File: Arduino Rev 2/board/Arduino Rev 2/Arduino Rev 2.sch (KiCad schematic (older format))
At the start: 0 parts

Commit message: finished Schematic
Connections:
- net labels added: D0_RX, D1_TX, RESET
- wire segments 4 -> 34
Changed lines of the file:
@@
 $Descr A4 11693 8268
 encoding utf-8
-Sheet 1 4
+Sheet 1 6
 Title ""
 Date ""
@@
 F19 "A4_SDA" I R 6450 4450 50
 F20 "A5_SCL" I R 6450 4550 50
-F21 "RESET" I L 4900 4600 50
+F21 "RESET" I L 4900 4500 50
 F22 "D0_RX" I L 4900 3250 50
 F23 "D1_TX" I L 4900 3350 50
@@
 F2 "TXD" I R 4000 3350 50
 F3 "RXD" I R 4000 3250 50
+F4 "DTR" I R 4000 3800 50
 $EndSheet
 Wire Wire Line
@@
 F0 "RESET" 50
 F1 "RESET.sch" 50
+F2 "RESET" I R 4050 4500 50
 $EndSheet
+Wire Wire Line
+	4050 4500 4500 4500
+Wire Wire Line
+	4000 3800 4500 3800
+Wire Wire Line
+	4500 3800 4500 4500
+Connection ~ 4500 4500
+Wire Wire Line
+	4500 4500 4900 4500
+Text Label 4150 4500 0    50   ~ 0
+RESET
+$Sheet
+S 7250 2500 1050 2700
+U 5F10049F
+F0 "PIN HEADERS" 50
+F1 "PIN HEADERS.sch" 50
+F2 "1" I L 7250 2550 50
+F3 "2" I L 7250 2650 50
+F4 "3" I L 7250 2750 50
+F5 "4" I L 7250 2850 50
+F6 "5" I L 7250 2950 50
+F7 "6" I L 7250 3050 50
+F8 "7" I L 7250 3150 50
+F9 "8" I L 7250 3250 50
+F10 "9" I L 7250 3350 50
+F11 "10" I L 7250 3450 50
+F12 "11" I L 7250 3550 50
+F13 "12" I L 7250 3650 50
+F14 "13" I L 7250 3750 50
+F15 "14" I L 7250 3850 50
+F16 "15" I L 7250 4050 50
+F17 "16" I L 7250 4150 50
+F18 "17" I L 7250 4250 50
+F19 "18" I L 7250 4350 50
+F20 "19" I L 7250 4450 50
+F21 "20" I L 7250 4550 50
+F22 "21" I L 7250 4650 50
+F23 "22" I L 7250 4750 50
+F24 "23" I L 7250 5000 50
+F25 "24" I L 7250 5100 50
+$EndSheet
+Wire Wire Line
+	6450 2750 7250 2750
+Wire Wire Line
+	7250 2850 6450 2850
+Wire Wire Line
+	6450 2950 7250 2950
+Wire Wire Line
+	7250 3050 6450 3050
+Wire Wire Line
+	6450 3150 7250 3150
+Wire Wire Line
+	7250 3250 6450 3250
+Wire Wire Line
+	6450 3350 7250 3350
+Wire Wire Line
+	7250 3450 6450 3450
+Wire Wire Line
+	6450 3550 7250 3550
+Wire Wire Line
+	7250 3650 6450 3650
+Wire Wire Line
+	6450 3750 7250 3750
+Wire Wire Line
+	7250 3850 6450 3850
+Wire Wire Line
+	6450 4050 7250 4050
+Wire Wire Line
+	7250 4150 6450 4150
+Wire Wire Line
+	6450 4250 7250 4250
+Wire Wire Line
+	7250 4350 6450 4350
+Wire Wire Line
+	6450 4450 7250 4450
+Wire Wire Line
+	7250 4550 6450 4550
+Wire Wire Line
+	6450 4650 7250 4650
+Wire Wire Line
+	7250 4750 6450 4750
+Wire Wire Line
+	6450 5050 6500 5050
+Wire Wire Line
+	6500 5050 6500 5000
+Wire Wire Line
+	6500 5000 7250 5000
+Wire Wire Line
+	7250 5100 6850 5100
+Wire Wire Line
+	7250 2650 6850 2650
+Wire Wire Line
+	7250 2550 6850 2550
+Text Label 6900 5100 0    50   ~ 0
+RESET
+Text Label 6950 2550 0    50   ~ 0
+D0_RX
+Text Label 6950 2650 0    50   ~ 0
+D1_TX
+Text Label 4300 3250 0    50   ~ 0
+D0_RX
+Text Label 4300 3350 0    50   ~ 0
+D1_TX
 $EndSCHEMATC

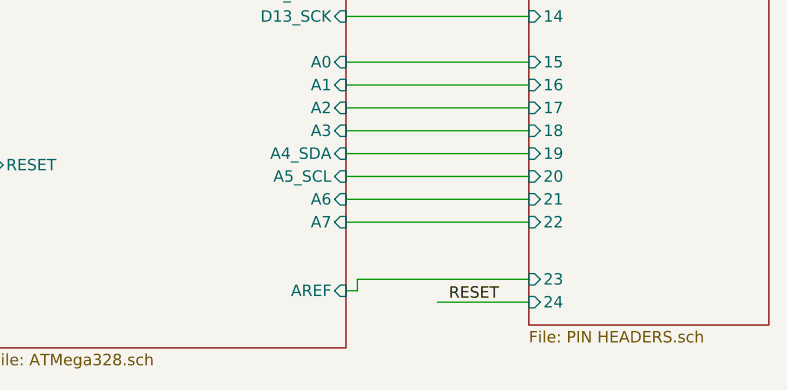
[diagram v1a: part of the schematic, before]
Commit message: Fixed Schematic. Routing Finished
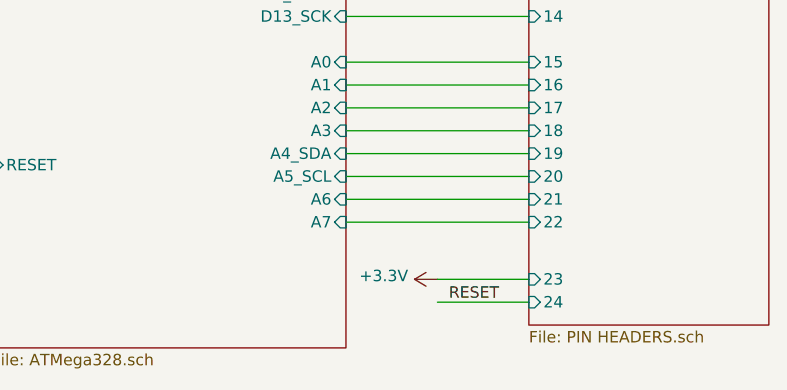
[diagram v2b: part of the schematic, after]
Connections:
- net labels added: +3.3V
- wire segments 34 -> 32
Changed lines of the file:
@@
 $EndDescr
-$Sheet
-S 4900 2100 1550 3200
-U 5F0BDC7A
-F0 "ATMega328" 50
-F1 "ATMega328.sch" 50
-F2 "D3" I R 6450 2850 50
-F3 "D4" I R 6450 2950 50
-F4 "XTAL1" I L 4900 2300 50
-F5 "XTAL2" I L 4900 2450 50
-F6 "D5" I R 6450 3050 50
-F7 "D6" I R 6450 3150 50
-F8 "D7" I R 6450 3250 50
-F9 "D8" I R 6450 3350 50
-F10 "D9" I R 6450 3450 50
-F11 "D10" I R 6450 3550 50
-F12 "D11_MOSI" I R 6450 3650 50
-F13 "D12_MISO" I R 6450 3750 50
-F14 "D13_SCK" I R 6450 3850 50
-F15 "A0" I R 6450 4050 50
-F16 "A1" I R 6450 4150 50
-F17 "A2" I R 6450 4250 50
-F18 "A3" I R 6450 4350 50
-F19 "A4_SDA" I R 6450 4450 50
-F20 "A5_SCL" I R 6450 4550 50
-F21 "RESET" I L 4900 4500 50
-F22 "D0_RX" I L 4900 3250 50
-F23 "D1_TX" I L 4900 3350 50
-F24 "D2" I R 6450 2750 50
-F25 "A6" I R 6450 4650 50
-F26 "AREF" I R 6450 5050 50
-F27 "A7" I R 6450 4750 50
-$EndSheet
 $Sheet
 S 3150 2200 850  350
@@
 	7250 4750 6450 4750
 Wire Wire Line
-	6450 5050 6500 5050
-Wire Wire Line
-	6500 5050 6500 5000
-Wire Wire Line
-	6500 5000 7250 5000
-Wire Wire Line
 	7250 5100 6850 5100
 Wire Wire Line
@@
 Text Label 4300 3350 0    50   ~ 0
 D1_TX
+$Sheet
+S 4900 2100 1550 3200
+U 5F0BDC7A
+F0 "ATMega328" 50
+F1 "ATMega328.sch" 50
+F2 "D3" I R 6450 2850 50
+F3 "D4" I R 6450 2950 50
+F4 "XTAL1" I L 4900 2300 50
+F5 "XTAL2" I L 4900 2450 50
+F6 "D5" I R 6450 3050 50
+F7 "D6" I R 6450 3150 50
+F8 "D7" I R 6450 3250 50
+F9 "D8" I R 6450 3350 50
+F10 "D9" I R 6450 3450 50
+F11 "D10" I R 6450 3550 50
+F12 "D11_MOSI" I R 6450 3650 50
+F13 "D12_MISO" I R 6450 3750 50
+F14 "D13_SCK" I R 6450 3850 50
+F15 "A0" I R 6450 4050 50
+F16 "A1" I R 6450 4150 50
+F17 "A2" I R 6450 4250 50
+F18 "A3" I R 6450 4350 50
+F19 "A4_SDA" I R 6450 4450 50
+F20 "A5_SCL" I R 6450 4550 50
+F21 "RESET" I L 4900 4500 50
+F22 "D0_RX" I L 4900 3250 50
+F23 "D1_TX" I L 4900 3350 50
+F24 "D2" I R 6450 2750 50
+F25 "A6" I R 6450 4650 50
+F26 "A7" I R 6450 4750 50
+$EndSheet
+$Comp
+L power:+3.3V #PWR0101
+U 1 1 5F135A34
+P 6850 5000
+F 0 "#PWR0101" H 6850 4850 50  0001 C CNN
+F 1 "+3.3V" V 6865 5128 50  0000 L CNN
+F 2 "" H 6850 5000 50  0001 C CNN
+F 3 "" H 6850 5000 50  0001 C CNN
+	1    6850 5000
+	0    -1   -1   0
+$EndComp
+Wire Wire Line
+	7250 5000 6850 5000
 $EndSCHEMATC
